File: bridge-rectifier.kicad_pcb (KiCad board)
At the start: 2 copper layers, 70 x 114 mm, 10 parts, among them J1 LIVE, J2 +VE, J3 -VE, J4 EARTH, J5 EARTH

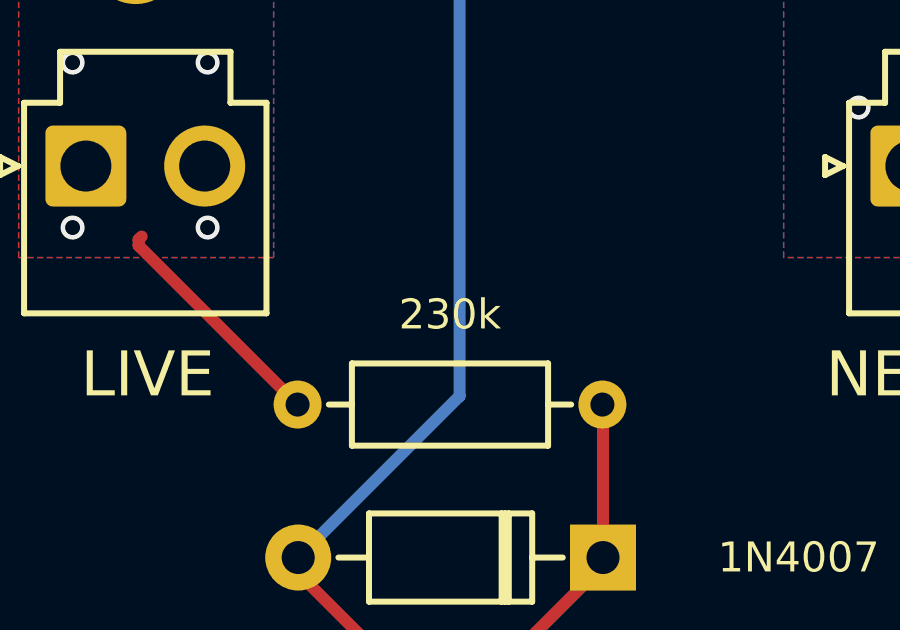
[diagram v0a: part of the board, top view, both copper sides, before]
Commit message: Change resistor to a standard value & remove unnecessary dimension
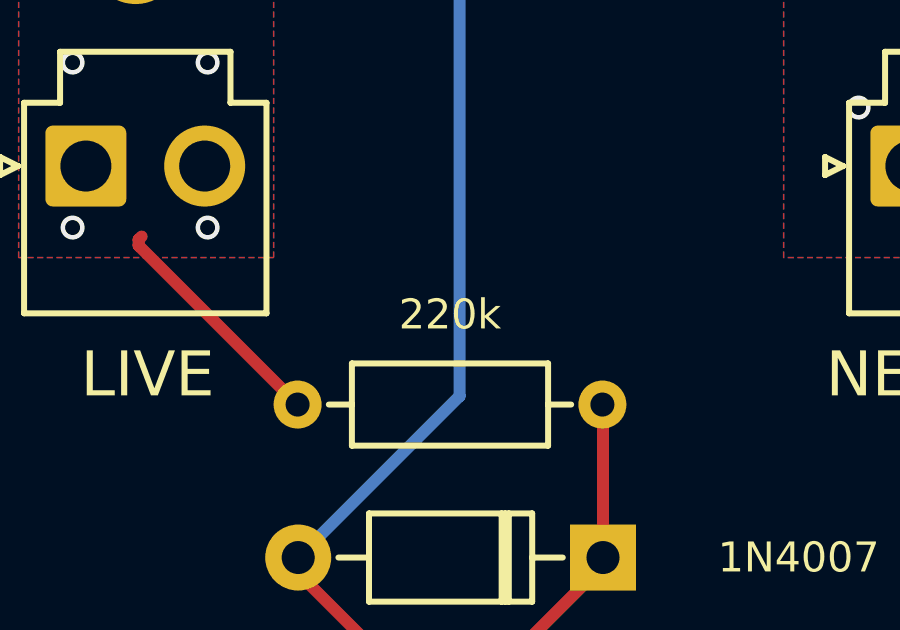
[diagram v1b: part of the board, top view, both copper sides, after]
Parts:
- R1: value 230k -> 220k
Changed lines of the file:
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@@
       (effects (font (size 1 1) (thickness 0.15)))
     )
-    (fp_text value "230k" (at 5.08 -3 180) (layer "F.SilkS")
+    (fp_text value "220k" (at 5.08 -3 180) (layer "F.SilkS")
       (effects (font (size 1 1) (thickness 0.15)))
     )
@@
     (effects (font (size 1 1) (thickness 0.15)))
   )
-  (dimension (type aligned) (layer "Dwgs.User")
-    (pts (xy 152.34808 39) (xy 152.34808 14))
-    (height -30)
-    (gr_text "25.0000 mm" (at 121.19808 26.5 90) (layer "Dwgs.User")
-      (effects (font (size 1 1) (thickness 0.15)))
-    )
-    (format (units 3) (units_format 1) (precision 4))
-    (style (thickness 0.1) (arrow_length 1.27) (text_position_mode 0) (extension_height 0.58642) (extension_offset 0.5) keep_text_aligned)
-  )
   (segment (start 162.48 119.26) (end 162.48 119) (width 0.4) (layer "F.Cu") (net 1))
